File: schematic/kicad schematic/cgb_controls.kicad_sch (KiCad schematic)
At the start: 8 parts, among them SW2 Right, SW3 Down, SW4 Up, SW5 Left, SW6 A, SW7 B, SW8 Select, SW9 Start

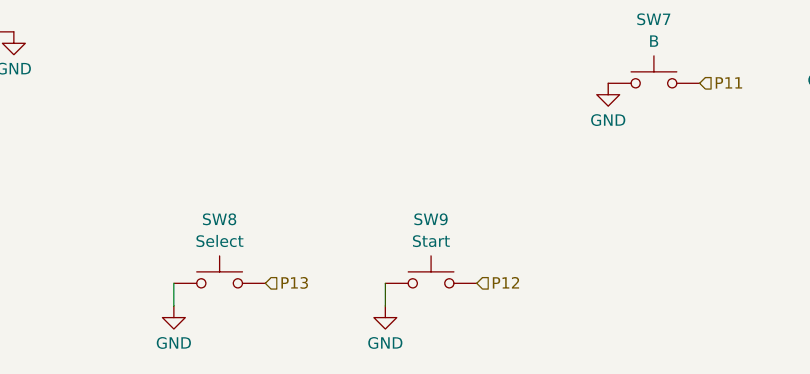
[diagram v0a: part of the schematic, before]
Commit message: fixed schematic, thx giltesa and darren
the ir transistor was labelled wrong
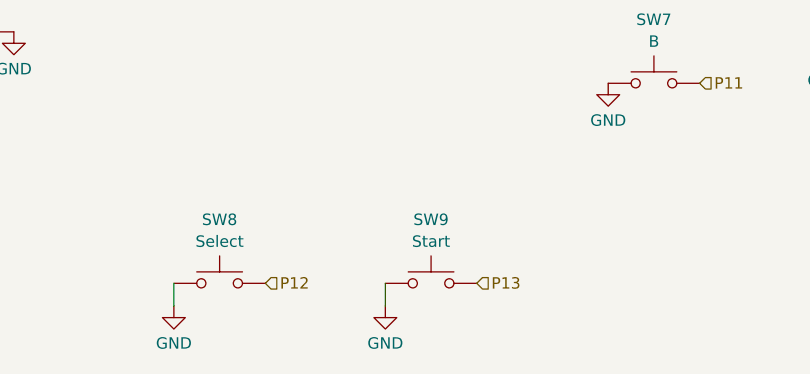
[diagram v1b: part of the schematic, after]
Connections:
- net P12: now also SW8.2; no longer SW9.2
- net P13: now also SW9.2; no longer SW8.2
